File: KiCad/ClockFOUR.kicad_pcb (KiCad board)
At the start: 2 copper layers, 220 x 240 mm, 6 parts, among them SW1 SW_RST, U1 DS3231N

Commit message: Board layout updated
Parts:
- removed SW1: SW_RST, SW_PUSH_SMALL
- added BT1: BATT_RTC, CR2032, F.Cu at (247.5, 36.8)
- added C11: 100n, C4_SM0805, F.Cu at (57.5, 59.0)
- added C12: 100n, C4_SM0805, F.Cu at (72.8, 59.0)
- added C13: 100n, C4_SM0805, F.Cu at (87.5, 59.0)
- added C14: 100n, C4_SM0805, F.Cu at (102.5, 59.0)
- added C15: 100n, C4_SM0805, F.Cu at (117.5, 59.0)
- added C16: 100n, C4_SM0805, F.Cu at (132.5, 59.0)
- added C17: 100n, C4_SM0805, F.Cu at (147.5, 59.0)
- added C18: 100n, C4_SM0805, F.Cu at (162.5, 59.0)
- added C19: 100n, C4_SM0805, F.Cu at (177.5, 59.0)
- added C20: 100n, C4_SM0805, F.Cu at (192.5, 59.0)
- added C21: 100n, C4_SM0805, F.Cu at (207.5, 59.0)
- added C22: 100n, C4_SM0805, F.Cu at (222.5, 59.0)
- added C23: 100n, C4_SM0805, F.Cu at (237.5, 59.0)
- added C24: 100n, C4_SM0805, F.Cu at (252.5, 59.0)
- added LED1: WS2812B, WS2812B, F.Cu at (61.5, 59.0)
- added LED10: WS2812B, WS2812B, F.Cu at (196.5, 59.0)
- added LED11: WS2812B, WS2812B, F.Cu at (211.5, 59.0)
- added LED12: WS2812B, WS2812B, F.Cu at (226.5, 59.0)
- added LED13: WS2812B, WS2812B, F.Cu at (241.5, 59.0)
- added LED14: WS2812B, WS2812B, F.Cu at (256.5, 59.0)
- added LED2: WS2812B, WS2812B, F.Cu at (76.5, 59.0)
- added LED3: WS2812B, WS2812B, F.Cu at (91.5, 59.0)
- added LED4: WS2812B, WS2812B, F.Cu at (106.5, 59.0)
- added LED5: WS2812B, WS2812B, F.Cu at (121.5, 59.0)
- added LED6: WS2812B, WS2812B, F.Cu at (136.5, 59.0)
- added LED7: WS2812B, WS2812B, F.Cu at (151.5, 59.0)
- added LED8: WS2812B, WS2812B, F.Cu at (166.5, 59.0)
- added LED9: WS2812B, WS2812B, F.Cu at (181.5, 59.0)
- U1: value DS3231N -> ATMEGA328P; footprint so-16 -> TQFP32
- moved S1 312.8 mm to (59.0, 46.0)
- moved U1 248.2 mm to (188.0, 37.2)
- moved S2 223.0 mm to (259.0, 46.0)
- moved S3 220.4 mm to (59.0, 264.0)
- moved S4 20.8 mm to (259.0, 264.0)
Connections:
- U1 pad 1: N-0000051 -> (no net)
- U1 pad 10: GND -> (no net)
- U1 pad 11: GND -> (no net)
- U1 pad 12: GND -> (no net)
- U1 pad 13: GND -> (no net)
- U1 pad 14: N-000006 -> (no net)
- U1 pad 15: /SDA -> (no net)
- U1 pad 16: /SCL -> (no net)
- U1 pad 2: 5V -> (no net)
- U1 pad 3: N-0000052 -> (no net)
- U1 pad 4: /RESET -> (no net)
- U1 pad 5: GND -> (no net)
- U1 pad 6: GND -> (no net)
- U1 pad 7: GND -> (no net)
- U1 pad 8: GND -> (no net)
- U1 pad 9: GND -> (no net)
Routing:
- net (no net): track 0.00 -> 373.9 mm
- net 5V: track 0.00 -> 234.7 mm
- net /Row_B/DI_B: track 0.00 -> 204.6 mm
- net N-0000098: track 0.00 -> 14.1 mm
- net N-0000097: track 0.00 -> 14.1 mm
- net N-0000096: track 0.00 -> 14.1 mm
- net N-0000095: track 0.00 -> 14.1 mm
- net N-0000094: track 0.00 -> 14.1 mm
- net N-0000093: track 0.00 -> 14.1 mm
- net N-0000092: track 0.00 -> 14.1 mm
- net N-0000091: track 0.00 -> 14.1 mm
- net N-0000090: track 0.00 -> 14.1 mm
- net N-0000089: track 0.00 -> 14.1 mm
- net N-0000088: track 0.00 -> 14.1 mm
- net N-0000087: track 0.00 -> 14.1 mm
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- added copper zone on F.Cu, net GND
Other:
- board size 220 x 240 mm -> 210 x 240 mm

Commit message: Board layout updated
Matrix placed and wired. Added RTC.
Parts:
- added C100: 100n, C4_SM0805, F.Cu at (117.8, 155.0)
- added C101: 100n, C4_SM0805, F.Cu at (132.8, 155.0)
- added C102: 100n, C4_SM0805, F.Cu at (147.8, 155.0)
- added C103: 100n, C4_SM0805, F.Cu at (162.8, 155.0)
- added C104: 100n, C4_SM0805, F.Cu at (177.8, 155.0)
- added C105: 100n, C4_SM0805, F.Cu at (192.8, 155.0)
- added C106: 100n, C4_SM0805, F.Cu at (207.8, 155.0)
- added C107: 100n, C4_SM0805, F.Cu at (222.8, 155.0)
- added C108: 100n, C4_SM0805, F.Cu at (237.8, 155.0)
- added C109: 100n, C4_SM0805, F.Cu at (252.8, 155.0)
- added C110: 100n, C4_SM0805, F.Cu at (57.8, 171.0)
- added C111: 100n, C4_SM0805, F.Cu at (72.8, 171.0)
- added C112: 100n, C4_SM0805, F.Cu at (87.8, 171.0)
- added C113: 100n, C4_SM0805, F.Cu at (102.8, 171.0)
- added C114: 100n, C4_SM0805, F.Cu at (117.8, 171.0)
- added C115: 100n, C4_SM0805, F.Cu at (132.8, 171.0)
- added C116: 100n, C4_SM0805, F.Cu at (147.8, 171.0)
- added C117: 100n, C4_SM0805, F.Cu at (162.8, 171.0)
- added C118: 100n, C4_SM0805, F.Cu at (177.8, 171.0)
- added C119: 100n, C4_SM0805, F.Cu at (192.8, 171.0)
- added C120: 100n, C4_SM0805, F.Cu at (207.8, 171.0)
- added C121: 100n, C4_SM0805, F.Cu at (222.8, 171.0)
- added C122: 100n, C4_SM0805, F.Cu at (237.8, 171.0)
- added C123: 100n, C4_SM0805, F.Cu at (252.8, 171.0)
- added C124: 100n, C4_SM0805, F.Cu at (57.8, 187.0)
- added C125: 100n, C4_SM0805, F.Cu at (72.8, 187.0)
- added C126: 100n, C4_SM0805, F.Cu at (87.8, 187.0)
- added C127: 100n, C4_SM0805, F.Cu at (102.8, 187.0)
- added C128: 100n, C4_SM0805, F.Cu at (117.8, 187.0)
- added C129: 100n, C4_SM0805, F.Cu at (132.8, 187.0)
- added C130: 100n, C4_SM0805, F.Cu at (147.8, 187.0)
- added C131: 100n, C4_SM0805, F.Cu at (162.8, 187.0)
- added C132: 100n, C4_SM0805, F.Cu at (177.8, 187.0)
- added C133: 100n, C4_SM0805, F.Cu at (192.8, 187.0)
- added C134: 100n, C4_SM0805, F.Cu at (207.8, 187.0)
- added C135: 100n, C4_SM0805, F.Cu at (222.8, 187.0)
- added C136: 100n, C4_SM0805, F.Cu at (237.8, 187.0)
- added C137: 100n, C4_SM0805, F.Cu at (252.8, 187.0)
- added C138: 100n, C4_SM0805, F.Cu at (57.8, 203.0)
- added C139: 100n, C4_SM0805, F.Cu at (72.8, 203.0)
- added C140: 100n, C4_SM0805, F.Cu at (87.8, 203.0)
- added C141: 100n, C4_SM0805, F.Cu at (102.8, 203.0)
- added C142: 100n, C4_SM0805, F.Cu at (117.8, 203.0)
- added C143: 100n, C4_SM0805, F.Cu at (132.8, 203.0)
- added C144: 100n, C4_SM0805, F.Cu at (147.8, 203.0)
- added C145: 100n, C4_SM0805, F.Cu at (162.8, 203.0)
- added C146: 100n, C4_SM0805, F.Cu at (177.8, 203.0)
- added C147: 100n, C4_SM0805, F.Cu at (192.8, 203.0)
- added C148: 100n, C4_SM0805, F.Cu at (207.8, 203.0)
- added C149: 100n, C4_SM0805, F.Cu at (222.8, 203.0)
- added C150: 100n, C4_SM0805, F.Cu at (237.8, 203.0)
- added C151: 100n, C4_SM0805, F.Cu at (252.8, 203.0)
- added C152: 100n, C4_SM0805, F.Cu at (57.8, 219.0)
- added C153: 100n, C4_SM0805, F.Cu at (72.8, 219.0)
- added C154: 100n, C4_SM0805, F.Cu at (87.8, 219.0)
- added C155: 100n, C4_SM0805, F.Cu at (102.8, 219.0)
- added C156: 100n, C4_SM0805, F.Cu at (117.8, 219.0)
- added C157: 100n, C4_SM0805, F.Cu at (132.8, 219.0)
- added C158: 100n, C4_SM0805, F.Cu at (147.8, 219.0)
- added C159: 100n, C4_SM0805, F.Cu at (162.8, 219.0)
- added C160: 100n, C4_SM0805, F.Cu at (177.8, 219.0)
- added C161: 100n, C4_SM0805, F.Cu at (192.8, 219.0)
- added C162: 100n, C4_SM0805, F.Cu at (207.8, 219.0)
- added C163: 100n, C4_SM0805, F.Cu at (222.8, 219.0)
- added C164: 100n, C4_SM0805, F.Cu at (237.8, 219.0)
- added C165: 100n, C4_SM0805, F.Cu at (252.8, 219.0)
- added C166: 100n, C4_SM0805, F.Cu at (57.8, 235.0)
- added C167: 100n, C4_SM0805, F.Cu at (72.8, 235.0)
- added C168: 100n, C4_SM0805, F.Cu at (87.8, 235.0)
- added C169: 100n, C4_SM0805, F.Cu at (102.8, 235.0)
- added C170: 100n, C4_SM0805, F.Cu at (117.8, 235.0)
- added C171: 100n, C4_SM0805, F.Cu at (132.8, 235.0)
- added C172: 100n, C4_SM0805, F.Cu at (147.8, 235.0)
- added C173: 100n, C4_SM0805, F.Cu at (162.8, 235.0)
- added C174: 100n, C4_SM0805, F.Cu at (177.8, 235.0)
- added C175: 100n, C4_SM0805, F.Cu at (192.8, 235.0)
- added C176: 100n, C4_SM0805, F.Cu at (207.8, 235.0)
- added C177: 100n, C4_SM0805, F.Cu at (222.8, 235.0)
- added C178: 100n, C4_SM0805, F.Cu at (237.8, 235.0)
- added C179: 100n, C4_SM0805, F.Cu at (252.8, 235.0)
- added C180: 100n, C4_SM0805, F.Cu at (57.8, 251.0)
- added C181: 100n, C4_SM0805, F.Cu at (72.8, 251.0)
- added C182: 100n, C4_SM0805, F.Cu at (87.8, 251.0)
- added C183: 100n, C4_SM0805, F.Cu at (102.8, 251.0)
- added C184: 100n, C4_SM0805, F.Cu at (117.8, 251.0)
- added C185: 100n, C4_SM0805, F.Cu at (132.8, 251.0)
- added C186: 100n, C4_SM0805, F.Cu at (147.8, 251.0)
- added C187: 100n, C4_SM0805, F.Cu at (162.8, 251.0)
- added C188: 100n, C4_SM0805, F.Cu at (177.8, 251.0)
- added C189: 100n, C4_SM0805, F.Cu at (192.8, 251.0)
- added C190: 100n, C4_SM0805, F.Cu at (207.8, 251.0)
- added C191: 100n, C4_SM0805, F.Cu at (222.8, 251.0)
- added C192: 100n, C4_SM0805, F.Cu at (237.8, 251.0)
- added C193: 100n, C4_SM0805, F.Cu at (252.8, 251.0)
- added C25: 100n, C4_SM0805, F.Cu at (252.8, 59.0)
- added C26: 100n, C4_SM0805, F.Cu at (57.8, 75.0)
- added C27: 100n, C4_SM0805, F.Cu at (72.8, 75.0)
- added C28: 100n, C4_SM0805, F.Cu at (87.8, 75.0)
- added C29: 100n, C4_SM0805, F.Cu at (102.8, 75.0)
- added C30: 100n, C4_SM0805, F.Cu at (117.8, 75.0)
- added C31: 100n, C4_SM0805, F.Cu at (132.8, 75.0)
- added C32: 100n, C4_SM0805, F.Cu at (147.8, 75.0)
- added C33: 100n, C4_SM0805, F.Cu at (162.8, 75.0)
- added C34: 100n, C4_SM0805, F.Cu at (177.8, 75.0)
- added C35: 100n, C4_SM0805, F.Cu at (192.8, 75.0)
- added C36: 100n, C4_SM0805, F.Cu at (207.8, 75.0)
- added C37: 100n, C4_SM0805, F.Cu at (222.8, 75.0)
- added C38: 100n, C4_SM0805, F.Cu at (237.8, 75.0)
- added C39: 100n, C4_SM0805, F.Cu at (252.8, 75.0)
- added C40: 100n, C4_SM0805, F.Cu at (57.8, 91.0)
- added C41: 100n, C4_SM0805, F.Cu at (72.8, 91.0)
- added C42: 100n, C4_SM0805, F.Cu at (87.8, 91.0)
- added C43: 100n, C4_SM0805, F.Cu at (102.8, 91.0)
- added C44: 100n, C4_SM0805, F.Cu at (117.8, 91.0)
- added C45: 100n, C4_SM0805, F.Cu at (132.8, 91.0)
- added C46: 100n, C4_SM0805, F.Cu at (147.8, 91.0)
- added C47: 100n, C4_SM0805, F.Cu at (162.8, 91.0)
- added C48: 100n, C4_SM0805, F.Cu at (177.5, 91.0)
- added C49: 100n, C4_SM0805, F.Cu at (192.8, 91.0)
- added C50: 100n, C4_SM0805, F.Cu at (207.8, 91.0)
- added C51: 100n, C4_SM0805, F.Cu at (222.8, 91.0)
- added C52: 100n, C4_SM0805, F.Cu at (237.8, 91.0)
- added C53: 100n, C4_SM0805, F.Cu at (252.8, 91.0)
- added C54: 100n, C4_SM0805, F.Cu at (57.8, 107.0)
- added C55: 100n, C4_SM0805, F.Cu at (72.8, 107.0)
- added C56: 100n, C4_SM0805, F.Cu at (87.8, 107.0)
- added C57: 100n, C4_SM0805, F.Cu at (102.8, 107.0)
- added C58: 100n, C4_SM0805, F.Cu at (117.8, 107.0)
- added C59: 100n, C4_SM0805, F.Cu at (132.8, 107.0)
- added C60: 100n, C4_SM0805, F.Cu at (147.8, 107.0)
- added C61: 100n, C4_SM0805, F.Cu at (162.8, 107.0)
- added C62: 100n, C4_SM0805, F.Cu at (177.8, 107.0)
- added C63: 100n, C4_SM0805, F.Cu at (192.8, 107.0)
- added C64: 100n, C4_SM0805, F.Cu at (207.8, 107.0)
- added C65: 100n, C4_SM0805, F.Cu at (222.8, 107.0)
- added C66: 100n, C4_SM0805, F.Cu at (237.8, 107.0)
- added C67: 100n, C4_SM0805, F.Cu at (252.8, 107.0)
- added C68: 100n, C4_SM0805, F.Cu at (57.8, 123.0)
- added C69: 100n, C4_SM0805, F.Cu at (72.8, 123.0)
- added C70: 100n, C4_SM0805, F.Cu at (87.8, 123.0)
- added C71: 100n, C4_SM0805, F.Cu at (102.8, 123.0)
- added C72: 100n, C4_SM0805, F.Cu at (117.8, 123.0)
- added C73: 100n, C4_SM0805, F.Cu at (132.8, 123.0)
- added C74: 100n, C4_SM0805, F.Cu at (147.8, 123.0)
- added C75: 100n, C4_SM0805, F.Cu at (162.8, 123.0)
- added C76: 100n, C4_SM0805, F.Cu at (177.8, 123.0)
- added C77: 100n, C4_SM0805, F.Cu at (192.8, 123.0)
- added C78: 100n, C4_SM0805, F.Cu at (207.8, 123.0)
- added C79: 100n, C4_SM0805, F.Cu at (222.8, 123.0)
- added C80: 100n, C4_SM0805, F.Cu at (237.8, 123.0)
- added C81: 100n, C4_SM0805, F.Cu at (252.8, 123.0)
- added C82: 100n, C4_SM0805, F.Cu at (57.8, 139.0)
- added C83: 100n, C4_SM0805, F.Cu at (72.8, 139.0)
- added C84: 100n, C4_SM0805, F.Cu at (87.8, 139.0)
- added C85: 100n, C4_SM0805, F.Cu at (102.8, 139.0)
- added C86: 100n, C4_SM0805, F.Cu at (117.8, 139.0)
- added C87: 100n, C4_SM0805, F.Cu at (132.8, 139.0)
- added C88: 100n, C4_SM0805, F.Cu at (147.8, 139.0)
- added C89: 100n, C4_SM0805, F.Cu at (162.8, 139.0)
- added C9: 100n, SM0805, B.Cu at (98.2, 46.2)
- added C90: 100n, C4_SM0805, F.Cu at (177.8, 139.0)
- added C91: 100n, C4_SM0805, F.Cu at (192.8, 139.0)
- added C92: 100n, C4_SM0805, F.Cu at (207.8, 139.0)
- added C93: 100n, C4_SM0805, F.Cu at (222.8, 139.0)
- added C94: 100n, C4_SM0805, F.Cu at (237.8, 139.0)
- added C95: 100n, C4_SM0805, F.Cu at (252.8, 139.0)
- added C96: 100n, C4_SM0805, F.Cu at (57.8, 155.0)
- added C97: 100n, C4_SM0805, F.Cu at (72.8, 155.0)
- added C98: 100n, C4_SM0805, F.Cu at (87.8, 155.0)
- added C99: 100n, C4_SM0805, F.Cu at (102.8, 155.0)
- added LED100: WS2812B, WS2812B, F.Cu at (76.5, 171.0)
- added LED101: WS2812B, WS2812B, F.Cu at (91.5, 171.0)
- added LED102: WS2812B, WS2812B, F.Cu at (106.5, 171.0)
- added LED103: WS2812B, WS2812B, F.Cu at (121.5, 171.0)
- added LED104: WS2812B, WS2812B, F.Cu at (136.5, 171.0)
- added LED105: WS2812B, WS2812B, F.Cu at (151.5, 171.0)
- added LED106: WS2812B, WS2812B, F.Cu at (166.5, 171.0)
- added LED107: WS2812B, WS2812B, F.Cu at (181.5, 171.0)
- added LED108: WS2812B, WS2812B, F.Cu at (196.5, 171.0)
- added LED109: WS2812B, WS2812B, F.Cu at (211.5, 171.0)
- added LED110: WS2812B, WS2812B, F.Cu at (226.5, 171.0)
- added LED111: WS2812B, WS2812B, F.Cu at (241.5, 171.0)
- added LED112: WS2812B, WS2812B, F.Cu at (256.5, 171.0)
- added LED113: WS2812B, WS2812B, F.Cu at (61.5, 187.0)
- added LED114: WS2812B, WS2812B, F.Cu at (76.5, 187.0)
- added LED115: WS2812B, WS2812B, F.Cu at (91.5, 187.0)
- added LED116: WS2812B, WS2812B, F.Cu at (106.5, 187.0)
- added LED117: WS2812B, WS2812B, F.Cu at (121.5, 187.0)
- added LED118: WS2812B, WS2812B, F.Cu at (136.5, 187.0)
- added LED119: WS2812B, WS2812B, F.Cu at (151.5, 187.0)
- added LED120: WS2812B, WS2812B, F.Cu at (166.5, 187.0)
- added LED121: WS2812B, WS2812B, F.Cu at (181.5, 187.0)
- added LED122: WS2812B, WS2812B, F.Cu at (196.5, 187.0)
- added LED123: WS2812B, WS2812B, F.Cu at (211.5, 187.0)
- added LED124: WS2812B, WS2812B, F.Cu at (226.5, 187.0)
- added LED125: WS2812B, WS2812B, F.Cu at (241.5, 187.0)
- added LED126: WS2812B, WS2812B, F.Cu at (256.5, 187.0)
- added LED127: WS2812B, WS2812B, F.Cu at (61.5, 203.0)
- added LED128: WS2812B, WS2812B, F.Cu at (76.5, 203.0)
- added LED129: WS2812B, WS2812B, F.Cu at (91.5, 203.0)
- added LED130: WS2812B, WS2812B, F.Cu at (106.5, 203.0)
- added LED131: WS2812B, WS2812B, F.Cu at (121.5, 203.0)
- added LED132: WS2812B, WS2812B, F.Cu at (136.5, 203.0)
- added LED133: WS2812B, WS2812B, F.Cu at (151.5, 203.0)
- added LED134: WS2812B, WS2812B, F.Cu at (166.5, 203.0)
- added LED135: WS2812B, WS2812B, F.Cu at (181.5, 203.0)
- added LED136: WS2812B, WS2812B, F.Cu at (196.5, 203.0)
- added LED137: WS2812B, WS2812B, F.Cu at (211.5, 203.0)
- added LED138: WS2812B, WS2812B, F.Cu at (226.5, 203.0)
- added LED139: WS2812B, WS2812B, F.Cu at (241.5, 203.0)
- added LED140: WS2812B, WS2812B, F.Cu at (256.5, 203.0)
- added LED141: WS2812B, WS2812B, F.Cu at (61.5, 219.0)
- added LED142: WS2812B, WS2812B, F.Cu at (76.5, 219.0)
- added LED143: WS2812B, WS2812B, F.Cu at (91.5, 219.0)
- added LED144: WS2812B, WS2812B, F.Cu at (106.5, 219.0)
- added LED145: WS2812B, WS2812B, F.Cu at (121.5, 219.0)
- added LED146: WS2812B, WS2812B, F.Cu at (136.5, 219.0)
- added LED147: WS2812B, WS2812B, F.Cu at (151.5, 219.0)
- added LED148: WS2812B, WS2812B, F.Cu at (166.5, 219.0)
- added LED149: WS2812B, WS2812B, F.Cu at (181.5, 219.0)
- added LED15: WS2812B, WS2812B, F.Cu at (61.5, 75.0)
- added LED150: WS2812B, WS2812B, F.Cu at (196.5, 219.0)
- added LED151: WS2812B, WS2812B, F.Cu at (211.5, 219.0)
- added LED152: WS2812B, WS2812B, F.Cu at (226.5, 219.0)
- added LED153: WS2812B, WS2812B, F.Cu at (241.5, 219.0)
- added LED154: WS2812B, WS2812B, F.Cu at (256.5, 219.0)
- added LED155: WS2812B, WS2812B, F.Cu at (61.5, 235.0)
- added LED156: WS2812B, WS2812B, F.Cu at (76.5, 235.0)
- added LED157: WS2812B, WS2812B, F.Cu at (91.5, 235.0)
- added LED158: WS2812B, WS2812B, F.Cu at (106.5, 235.0)
- added LED159: WS2812B, WS2812B, F.Cu at (121.5, 235.0)
- added LED16: WS2812B, WS2812B, F.Cu at (76.5, 75.0)
- added LED160: WS2812B, WS2812B, F.Cu at (136.5, 235.0)
- added LED161: WS2812B, WS2812B, F.Cu at (151.5, 235.0)
- added LED162: WS2812B, WS2812B, F.Cu at (166.5, 235.0)
- added LED163: WS2812B, WS2812B, F.Cu at (181.5, 235.0)
- added LED164: WS2812B, WS2812B, F.Cu at (196.5, 235.0)
- added LED165: WS2812B, WS2812B, F.Cu at (211.5, 235.0)
- added LED166: WS2812B, WS2812B, F.Cu at (226.5, 235.0)
- added LED167: WS2812B, WS2812B, F.Cu at (241.5, 235.0)
- added LED168: WS2812B, WS2812B, F.Cu at (256.5, 235.0)
- added LED169: WS2812B, WS2812B, F.Cu at (61.5, 251.0)
- added LED17: WS2812B, WS2812B, F.Cu at (91.5, 75.0)
- added LED170: WS2812B, WS2812B, F.Cu at (76.5, 251.0)
- added LED171: WS2812B, WS2812B, F.Cu at (91.5, 251.0)
- added LED172: WS2812B, WS2812B, F.Cu at (106.5, 251.0)
- added LED173: WS2812B, WS2812B, F.Cu at (121.5, 251.0)
- added LED174: WS2812B, WS2812B, F.Cu at (136.5, 251.0)
- added LED175: WS2812B, WS2812B, F.Cu at (151.5, 251.0)
- added LED176: WS2812B, WS2812B, F.Cu at (166.5, 251.0)
- added LED177: WS2812B, WS2812B, F.Cu at (181.5, 251.0)
- added LED178: WS2812B, WS2812B, F.Cu at (196.5, 251.0)
- added LED179: WS2812B, WS2812B, F.Cu at (211.5, 251.0)
- added LED18: WS2812B, WS2812B, F.Cu at (106.5, 75.0)
- added LED180: WS2812B, WS2812B, F.Cu at (226.5, 251.0)
- added LED181: WS2812B, WS2812B, F.Cu at (241.5, 251.0)
- added LED182: WS2812B, WS2812B, F.Cu at (256.5, 251.0)
- added LED19: WS2812B, WS2812B, F.Cu at (121.5, 75.0)
- added LED20: WS2812B, WS2812B, F.Cu at (136.5, 75.0)
- added LED21: WS2812B, WS2812B, F.Cu at (151.5, 75.0)
- added LED22: WS2812B, WS2812B, F.Cu at (166.5, 75.0)
- added LED23: WS2812B, WS2812B, F.Cu at (181.5, 75.0)
- added LED24: WS2812B, WS2812B, F.Cu at (196.5, 75.0)
- added LED25: WS2812B, WS2812B, F.Cu at (211.5, 75.0)
- added LED26: WS2812B, WS2812B, F.Cu at (226.5, 75.0)
- added LED27: WS2812B, WS2812B, F.Cu at (241.5, 75.0)
- added LED28: WS2812B, WS2812B, F.Cu at (256.5, 75.0)
- added LED29: WS2812B, WS2812B, F.Cu at (61.5, 91.0)
- added LED30: WS2812B, WS2812B, F.Cu at (76.5, 91.0)
- added LED31: WS2812B, WS2812B, F.Cu at (91.5, 91.0)
- added LED32: WS2812B, WS2812B, F.Cu at (106.5, 91.0)
- added LED33: WS2812B, WS2812B, F.Cu at (121.5, 91.0)
- added LED34: WS2812B, WS2812B, F.Cu at (136.5, 91.0)
- added LED35: WS2812B, WS2812B, F.Cu at (151.5, 91.0)
- added LED36: WS2812B, WS2812B, F.Cu at (166.5, 91.0)
- added LED37: WS2812B, WS2812B, F.Cu at (181.5, 91.0)
- added LED38: WS2812B, WS2812B, F.Cu at (196.5, 91.0)
- added LED39: WS2812B, WS2812B, F.Cu at (211.5, 91.0)
- added LED40: WS2812B, WS2812B, F.Cu at (226.5, 91.0)
- added LED41: WS2812B, WS2812B, F.Cu at (241.5, 91.0)
- added LED42: WS2812B, WS2812B, F.Cu at (256.5, 91.0)
- added LED43: WS2812B, WS2812B, F.Cu at (61.5, 107.0)
- added LED44: WS2812B, WS2812B, F.Cu at (76.5, 107.0)
- added LED45: WS2812B, WS2812B, F.Cu at (91.5, 107.0)
- added LED46: WS2812B, WS2812B, F.Cu at (106.5, 107.0)
- added LED47: WS2812B, WS2812B, F.Cu at (121.5, 107.0)
- added LED48: WS2812B, WS2812B, F.Cu at (136.5, 107.0)
- added LED49: WS2812B, WS2812B, F.Cu at (151.5, 107.0)
- added LED50: WS2812B, WS2812B, F.Cu at (166.5, 107.0)
- added LED51: WS2812B, WS2812B, F.Cu at (181.5, 107.0)
- added LED52: WS2812B, WS2812B, F.Cu at (196.5, 107.0)
- added LED53: WS2812B, WS2812B, F.Cu at (211.5, 107.0)
- added LED54: WS2812B, WS2812B, F.Cu at (226.5, 107.0)
- added LED55: WS2812B, WS2812B, F.Cu at (241.5, 107.0)
- added LED56: WS2812B, WS2812B, F.Cu at (256.5, 107.0)
- added LED57: WS2812B, WS2812B, F.Cu at (61.5, 123.0)
- added LED58: WS2812B, WS2812B, F.Cu at (76.5, 123.0)
- added LED59: WS2812B, WS2812B, F.Cu at (91.5, 123.0)
- added LED60: WS2812B, WS2812B, F.Cu at (106.5, 123.0)
- added LED61: WS2812B, WS2812B, F.Cu at (121.5, 123.0)
- added LED62: WS2812B, WS2812B, F.Cu at (136.5, 123.0)
- added LED63: WS2812B, WS2812B, F.Cu at (151.5, 123.0)
- added LED64: WS2812B, WS2812B, F.Cu at (166.5, 123.0)
- added LED65: WS2812B, WS2812B, F.Cu at (181.5, 123.0)
- added LED66: WS2812B, WS2812B, F.Cu at (196.5, 123.0)
- added LED67: WS2812B, WS2812B, F.Cu at (211.5, 123.0)
- added LED68: WS2812B, WS2812B, F.Cu at (226.5, 123.0)
- added LED69: WS2812B, WS2812B, F.Cu at (241.5, 123.0)
- added LED70: WS2812B, WS2812B, F.Cu at (256.5, 123.0)
- added LED71: WS2812B, WS2812B, F.Cu at (61.5, 139.0)
- added LED72: WS2812B, WS2812B, F.Cu at (76.5, 139.0)
- added LED73: WS2812B, WS2812B, F.Cu at (91.5, 139.0)
- added LED74: WS2812B, WS2812B, F.Cu at (106.5, 139.0)
- added LED75: WS2812B, WS2812B, F.Cu at (121.5, 139.0)
- added LED76: WS2812B, WS2812B, F.Cu at (136.5, 139.0)
- added LED77: WS2812B, WS2812B, F.Cu at (151.5, 139.0)
- added LED78: WS2812B, WS2812B, F.Cu at (166.5, 139.0)
- added LED79: WS2812B, WS2812B, F.Cu at (181.5, 139.0)
- added LED80: WS2812B, WS2812B, F.Cu at (196.5, 139.0)
- added LED81: WS2812B, WS2812B, F.Cu at (211.5, 139.0)
- added LED82: WS2812B, WS2812B, F.Cu at (226.5, 139.0)
- added LED83: WS2812B, WS2812B, F.Cu at (241.5, 139.0)
- added LED84: WS2812B, WS2812B, F.Cu at (256.5, 139.0)
- added LED85: WS2812B, WS2812B, F.Cu at (61.5, 155.0)
- added LED86: WS2812B, WS2812B, F.Cu at (76.5, 155.0)
- added LED87: WS2812B, WS2812B, F.Cu at (91.5, 155.0)
- added LED88: WS2812B, WS2812B, F.Cu at (106.5, 155.0)
- added LED89: WS2812B, WS2812B, F.Cu at (121.5, 155.0)
- added LED90: WS2812B, WS2812B, F.Cu at (136.5, 155.0)
- added LED91: WS2812B, WS2812B, F.Cu at (151.5, 155.0)
- added LED92: WS2812B, WS2812B, F.Cu at (166.5, 155.0)
- added LED93: WS2812B, WS2812B, F.Cu at (181.5, 155.0)
- added LED94: WS2812B, WS2812B, F.Cu at (196.5, 155.0)
- added LED95: WS2812B, WS2812B, F.Cu at (211.5, 155.0)
- added LED96: WS2812B, WS2812B, F.Cu at (226.5, 155.0)
- added LED97: WS2812B, WS2812B, F.Cu at (241.5, 155.0)
- added LED98: WS2812B, WS2812B, F.Cu at (256.5, 155.0)
- added LED99: WS2812B, WS2812B, F.Cu at (61.5, 171.0)
- added P4: FTDI, SIL-6, F.Cu at (234.0, 44.8)
- added P5: LDR_header, SIL-2, F.Cu at (159.0, 43.5)
- added R1: 500R, SM0805, F.Cu at (61.2, 54.2)
- added R6: 10K, SM0805, F.Cu at (101.8, 46.0)
- added R7: 10K, SM0805, F.Cu at (99.5, 46.0)
- added R8: 4K7, SM0805, F.Cu at (65.5, 46.2)
- added R9: 4K7, SM0805, F.Cu at (68.2, 46.2)
- added U2: DS3231N, ssop-16, F.Cu at (84.0, 46.5)
- BT1, U1: moved to B.Cu
- C11: footprint C4_SM0805 -> SM0805
- moved C11 192.6 mm to (249.8, 47.0)
- moved BT1 163.8 mm to (84.0, 46.0), turned to 180 degrees
- moved U1 119.3 mm to (161.0, 153.5)
- moved C12 15.0 mm to (57.8, 59.0)
- moved C13 15.0 mm to (72.5, 59.0)
- moved C14 15.0 mm to (87.5, 59.0)
- moved C15 15.0 mm to (102.5, 59.0)
- moved C16 15.0 mm to (117.5, 59.0)
- moved C17 15.0 mm to (132.5, 59.0)
- moved C18 15.0 mm to (147.5, 59.0)
- moved C19 15.0 mm to (162.5, 59.0)
- moved C20 15.0 mm to (177.5, 59.0)
- moved C21 15.0 mm to (192.5, 59.0)
- moved C22 15.0 mm to (207.5, 59.0)
- moved C23 15.0 mm to (222.5, 59.0)
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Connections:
- C11 pad 1: GND -> 5V
- C11 pad 2: 5V -> GND
- U1 pad 15: (no net) -> /MOSI
- U1 pad 16: (no net) -> /MISO
- U1 pad 17: (no net) -> /SCK
- U1 pad 18: (no net) -> 5V
- U1 pad 20: (no net) -> N-0000024
- U1 pad 21: (no net) -> GND
- U1 pad 23: (no net) -> /LDR_PIN
- U1 pad 24: (no net) -> /BUTTON_L
- U1 pad 25: (no net) -> /SENSE_PIN
- U1 pad 26: (no net) -> /BUTTON_R
- U1 pad 27: (no net) -> /SDA
- U1 pad 28: (no net) -> /SCL
- U1 pad 29: (no net) -> /RESET
- U1 pad 3: (no net) -> GND
- U1 pad 30: (no net) -> /RXD
- U1 pad 31: (no net) -> /TXD
- U1 pad 32: (no net) -> /MATRIX_PIN
- U1 pad 4: (no net) -> 5V
- U1 pad 5: (no net) -> GND
- U1 pad 6: (no net) -> 5V
- U1 pad 7: (no net) -> N-0000030
- U1 pad 8: (no net) -> N-0000034
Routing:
- net 5V: track 234.7 -> 3184.9 mm
- net (no net): track 373.9 -> 0.00 mm
- net /Row_J/DI_J: track 0.00 -> 207.4 mm
- net /Row_E/DI_E: track 0.00 -> 207.2 mm
- net /Row_L/DI_L: track 0.00 -> 207.2 mm
- net /Row_K/DI_K: track 0.00 -> 207.2 mm
- net /Row_I/DI_I: track 0.00 -> 207.2 mm
- net /Row_H/DI_H: track 0.00 -> 207.2 mm
- net /Row_G/DI_G: track 0.00 -> 207.2 mm
- net /Row_F/DI_F: track 0.00 -> 207.2 mm
- net /Row_M/DI_M: track 0.00 -> 207.1 mm
- net /Row_D/DI_D: track 0.00 -> 204.9 mm
- net /Row_C/DI_C: track 0.00 -> 204.8 mm
- net GND: track 0.00 -> 26.2 mm, vias 0 -> 1
- net N-000008: track 0.00 -> 19.2 mm
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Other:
- board size 210 x 240 mm -> 210 x 228 mm

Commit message: Layout updated
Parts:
- added C1: 100n, SM0805, B.Cu at (138.2, 82.5)
- added C10: 47u, c_2917, F.Cu at (76.2, 264.0)
- added C2: 100p, SM0805, F.Cu at (146.8, 48.2)
- added C3: 100n, SM0805, B.Cu at (136.2, 67.2)
- added C4: 100p, SM0805, F.Cu at (155.0, 48.2)
- added C5: 22p, SM0805, B.Cu at (140.0, 90.5)
- added C6: 100n, SM0805, F.Cu at (226.5, 47.2)
- added C7: 22p, SM0805, B.Cu at (127.2, 90.2)
- added C8: 100n, SM0805, B.Cu at (127.0, 48.5)
- added P1: ICSP, Header_ISP, B.Cu at (121.5, 48.8)
- added P2: FTDI, Header_FTDI, F.Cu at (219.0, 44.8)
- added P3: LDR_header, SIL-2, F.Cu at (195.2, 44.8)
- added R2: 10K, SM0805, F.Cu at (235.5, 46.0)
- added R3: 1M, SM0805, F.Cu at (149.5, 48.2)
- added R4: 1M, SM0805, F.Cu at (152.2, 48.0)
- added R5: 10K, SM0805, F.Cu at (199.8, 45.8)
- added SW1: SW_RST, SW_PUSH_SMALL, F.Cu at (241.5, 46.2)
- added X1: CRYSTAL, Xtal_SMD, B.Cu at (133.5, 88.2)
- P4: value FTDI -> Button_Header; footprint SIL-6 -> SIL-2
- P5: value LDR_header -> BARREL_JACK; footprint SIL-2 -> JACK_ALIM
- R6, R7, R8, R9: moved to B.Cu
- U2: footprint ssop-16 -> DS3231; moved to B.Cu
- moved C11 241.7 mm to (140.8, 262.8)
- moved P5 221.9 mm to (151.0, 265.2), turned to 180 degrees
- moved P4 83.2 mm to (150.8, 44.8)
- moved U1 82.2 mm to (136.5, 75.0), turned to 90 degrees
- moved R8 47.1 mm to (107.8, 67.0)
- moved R9 42.2 mm to (105.0, 67.0)
- moved R7 31.9 mm to (81.0, 72.0), turned to 90 degrees
- moved R6 30.6 mm to (81.0, 68.5), turned to 90 degrees
- moved U2 21.7 mm to (91.2, 67.0)
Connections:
- P4 pad 1: GND -> /BUTTON_L
- P4 pad 2: GND -> /BUTTON_R
- P5 pad 2: /LDR_PIN -> GND
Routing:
- net /RESET: track 3.67 -> 300.6 mm
- net 5V: track 3184.9 -> 3461.1 mm, vias 0 -> 4
- net /MATRIX_PIN: track 0.00 -> 119.3 mm, vias 0 -> 1
- net /TXD: track 0.00 -> 111.2 mm, vias 0 -> 1
- net /RXD: track 0.00 -> 109.0 mm, vias 0 -> 1
- net /LDR_PIN: track 0.00 -> 94.3 mm, vias 0 -> 3
- net /SDA: track 14.0 -> 87.0 mm, vias 1 -> 2
- net /SCL: track 18.8 -> 87.5 mm, vias 1 -> 2
- net N-0000025: track 12.5 -> 79.6 mm
- net /MOSI: track 0.00 -> 52.5 mm
- net /BUTTON_R: track 0.00 -> 45.3 mm, vias 0 -> 1
- net /BUTTON_L: track 0.00 -> 36.8 mm, vias 0 -> 1
- net /SCK: track 0.00 -> 31.8 mm, vias 0 -> 2
- net /SENSE_PIN: track 0.00 -> 30.5 mm, vias 0 -> 1
- net /MISO: track 0.00 -> 29.2 mm, vias 0 -> 2
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- added copper zone on B.Cu, net GND

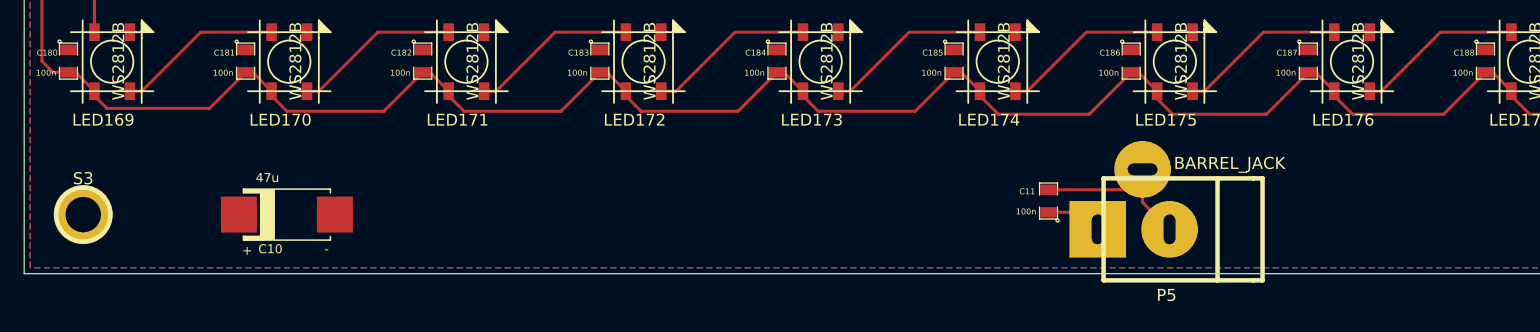
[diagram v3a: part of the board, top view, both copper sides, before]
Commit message: Layout updated
added 4x caps on power input.  Replace with single larger cap??
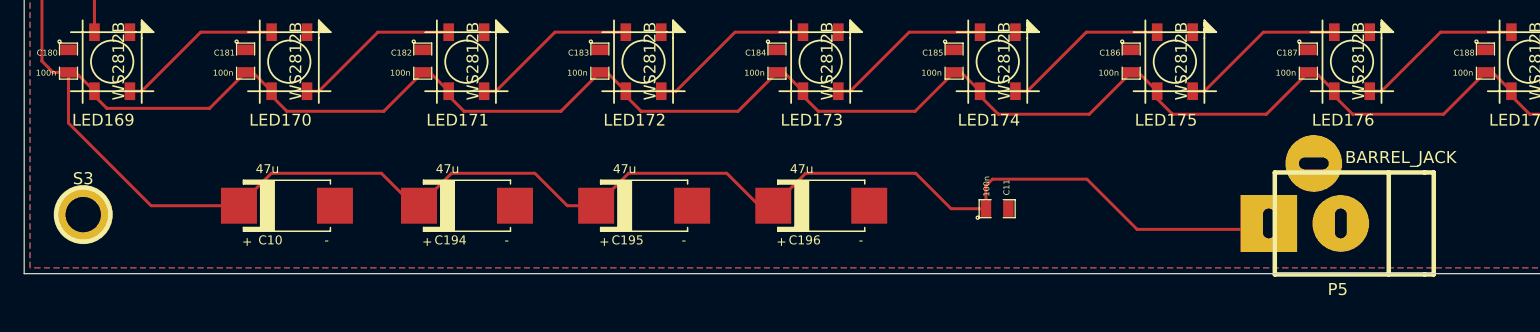
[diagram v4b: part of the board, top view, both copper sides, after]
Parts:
- added C194: 47u, c_2917, F.Cu at (91.5, 263.2)
- added C195: 47u, c_2917, F.Cu at (106.5, 263.2)
- added C196: 47u, c_2917, F.Cu at (121.5, 263.2)
- moved P5 14.5 mm to (165.5, 264.8)
- moved C11 4.32 mm to (136.5, 263.5), turned to 270 degrees
- moved C10 0.75 mm to (76.2, 263.2)
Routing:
- net 5V: track 3461.1 -> 3578.4 mm
- net GND: track 32.4 -> 17.7 mm
